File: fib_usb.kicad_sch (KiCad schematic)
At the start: 0 parts

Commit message: added several ICs, implementted schematics for charger, boost converter and LDOs
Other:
- note added: "TYPE-A 2.0"
- note added: "TYPE-C 2.0 DEBUG"
- note added: "TYPE-C HS DP"
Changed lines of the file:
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@@
 	(generator_version "8.0")
 	(paper "A4")
+	(text "TYPE-A 2.0"
+		(exclude_from_sim no)
+		(at 45.974 75.438 0)
+		(effects
+			(font
+				(size 1.27 1.27)
+			)
+		)
+	)
+	(text "TYPE-C HS DP"
+		(exclude_from_sim no)
+		(at 46.99 54.102 0)
+		(effects
+			(font
+				(size 1.27 1.27)
+			)
+		)
+	)
+	(text "TYPE-C 2.0 DEBUG"
+		(exclude_from_sim no)
+		(at 45.466 89.408 0)
+		(effects
+			(font
+				(size 1.27 1.27)
+			)
+		)
+	)
 )

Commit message: added usb+PD+DP & pcie implementations from antmicro design, added specs for USB components, rethought power+usb arch
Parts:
- added C100, C98: C_1u_16V_0402, jetson-orin-baseboard-footprints:C_0402_1005Metric, symbol jetson-orin-baseboard:C_1u_16V_0402
- added C56, C59, C67, C68, C80, C86, C96: C_10u_0402, jetson-orin-baseboard-footprints:C_0402_1005Metric, symbol jetson-orin-baseboard:C_10u_0402
- added C57, C70, C71, C72, C73, C74, C75, C76, C77, C78, C81, C82, C83, C84, C85, C89, C90, C91, C92, C94, C95, C97, C99: C_100n_0402, jetson-orin-baseboard-footprints:C_0402_1005Metric, symbol jetson-orin-baseboard:C_100n_0402
- added C69: C_10u_25V_0603, jetson-orin-baseboard-footprints:C_0603_1608Metric, symbol jetson-orin-baseboard:C_10u_25V_0603
- added C79, C93: C_4u7_25V_0402, jetson-orin-baseboard-footprints:C_0402_1005Metric, symbol jetson-orin-baseboard:C_4u7_25V_0402
- added C87, C88: C_47p_0402, jetson-orin-baseboard-footprints:C_0402_1005Metric, symbol jetson-orin-baseboard:C_47p_0402
- added D10, D12, D14, D7, D8, D9: LED_G_0603_LTST-C190GKT, jetson-orin-baseboard-footprints:LED_0603_1608Metric_G, symbol jetson-orin-baseboard:LED_G_0603_LTST-C190GKT
- added D11, D13: DF2S30FS_SOD, jetson-orin-baseboard-footprints:SOD-923, symbol jetson-orin-baseboard:DF2S30FS_SOD
- added D6: RB521S30T1G, jetson-orin-baseboard-footprints:SOD-523, symbol jetson-orin-baseboard:RB521S30T1G
- added J12: Conn_USB-C_WE_632723300011, jetson-orin-baseboard-footprints:Conn_USB-C_WE_632723300011, symbol jetson-orin-baseboard:USB-C_WE_632723300011
- added J8: USB-C_USB4105-GF-A, jetson-orin-baseboard-footprints:USB-C_GCT_USB4105-GF-A, symbol jetson-orin-baseboard:USB-C_GCT_USB4105-GF-A
- added R15, R17, R20, R52, R54, R60, R77: R_10k_0402, jetson-orin-baseboard-footprints:R_0402_1005Metric, symbol jetson-orin-baseboard:R_10k_0402
- added R16, R18, R48, R49: R_100k_0402, jetson-orin-baseboard-footprints:R_0402_1005Metric, symbol jetson-orin-baseboard:R_100k_0402
- added R19, R31, R32, R33, R34, R38, R41, R42, R43, R50, R51, R53, R55, R56, R75, R76: R_0R_0402, jetson-orin-baseboard-footprints:R_0402_1005Metric, symbol jetson-orin-baseboard:R_0R_0402
- added R27, R61, R62, R63, R64, R65, R66, R67, R68, R69, R70, R71, R72, R73, R74: R_1k_0402, jetson-orin-baseboard-footprints:R_0402_1005Metric, symbol jetson-orin-baseboard:R_1k_0402
- added R35, R36, R46, R47, R78, R98: R_4k7_0402, jetson-orin-baseboard-footprints:R_0402_1005Metric, symbol jetson-orin-baseboard:R_4k7_0402
- added R37: R_4x0R_0201_array, jetson-orin-baseboard-footprints:R_Array_4x0201_Panasonic_EXB18V, symbol jetson-orin-baseboard:R_4x0R_0201_array
- added R39, R40, R44, R45: R_200R_0402, jetson-orin-baseboard-footprints:R_0402_1005Metric, symbol jetson-orin-baseboard:R_200R_0402
- added R57, R79: R_2k2_0402, jetson-orin-baseboard-footprints:R_0402_1005Metric, symbol jetson-orin-baseboard:R_2k2_0402
- added R58, R59: R_27R_0402, jetson-orin-baseboard-footprints:R_0402_1005Metric, symbol jetson-orin-baseboard:R_27R_0402
- added R80, R97: R_2M_0402, jetson-orin-baseboard-footprints:R_0402_1005Metric, symbol jetson-orin-baseboard:R_2M_0402
- added TP1, TP10, TP11, TP2, TP3, TP4, TP5, TP6, TP7, TP8, TP9: TP_0.75mm_SMD, jetson-orin-baseboard-footprints:TP_SMD_0.75mm, symbol jetson-orin-baseboard:TP_0.75mm_SMD
- added U10: W25Q80DV_USON, jetson-orin-baseboard-footprints:USON-8_2x3mm_P0.5mm, symbol jetson-orin-baseboard:W25Q80DV_USON
- added U11, U13: AP22615A_TSOT26, jetson-orin-baseboard-footprints:TSOT23-6, symbol jetson-orin-baseboard:AP22615A_TSOT26
- added U12: TUSB1046-DCIRNQ, jetson-orin-baseboard-footprints:WQFN-40_1EP_6x3mm_Pitch0.4mm_EP4.7x2.7mm, symbol jetson-orin-baseboard:TUSB1046-DCIRNQ
- added U14, U15, U16, U17, U18: TPD4E05U06QDQARQ1, jetson-orin-baseboard-footprints:USON-10_2.5x1mm_P0.5mm, symbol jetson-orin-baseboard:TPD4E05U06QDQARQ1
- added U7: NCP730BMT330_WSON, jetson-orin-baseboard-footprints:WSON-6-1EP_2x2mm_P0.65mm, symbol jetson-orin-baseboard:NCP730BMT330_WSON
- added U8: TPS65988DHRSHR, jetson-orin-baseboard-footprints:IC_TPS65987DDHRSHR, symbol jetson-orin-baseboard:TPS65988DHRSHR
- added U9: FT230X_QFN, jetson-orin-baseboard-footprints:QFN-16-1EP_4x4mm_P0.65mm, symbol jetson-orin-baseboard:FT230X_QFN
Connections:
- new net: C72.1, R20.2, U9.9 (~{RESET})
- new net: R57.2, U11.5 (ISET)
- new net: R34.2, U9.4 (~{CTS})
- new net: D8.1, R39.2
- new net: TP9.1, U8.30 (GPIO3/HPD1)
- new net: D12.1, R78.2
- new net: TP11.1, U12.29 (CAD_SNK/RSVD1)
- new net: D9.1, R40.2
- new net: R53.2, R54.2, U11.4 (EN)
- new net: R31.2, U9.15 (TXD)
- new net: D7.1, R44.1
- new net: R79.2, U13.5 (ISET)
- new net: R32.2, U9.2 (RXD)
- new net: D10.1, R45.1
- new net: R76.2, R77.2, U13.4 (EN)
- new net: R33.2, U9.16 (~{RTS})
- new net: U14.4, U14.7
- new net: U14.5, U14.6
- new net: D14.1, R98.1
- new net +3V3: C56.1, C57.1, C74.1, C76.1, C78.1, C85.1, C86.1, R35.1, R36.1, R46.1, R47.1, R49.2, R60.2, R61.2, R63.2, R65.2, R67.2, R69.2, R71.2, R73.2, U12.1 (VCC), U12.20 (VCC), U12.28 (VCC), U12.6 (VCC), U8.5 (VIN_3V3)
- new net +5V: C75.1, C80.2, C90.1, C96.1, R50.2, R52.2, R75.2, U11.6 (IN), U13.6 (IN), U8.25 (PP1_CABLE), U8.46 (PP2_CABLE)
- new net DEBUG_RXD: R31.1
- new net DEBUG_TXD: R32.1
- new net DP1_AUX_N: R49.1, U12.25 (AUX_N)
- new net DP1_AUX_P: R48.1, U12.24 (AUX_P)
- new net DP1_TXD0_N: U12.10 (DP0_N)
- new net DP1_TXD0_P: U12.9 (DP0_P)
- new net DP1_TXD1_N: U12.13 (DP1_N)
- new net DP1_TXD1_P: U12.12 (DP1_P)
- new net DP1_TXD2_N: U12.16 (DP2_N)
- new net DP1_TXD2_P: U12.15 (DP2_P)
- new net DP1_TXD3_N: U12.19 (DP3_N)
- new net DP1_TXD3_P: U12.18 (DP3_P)
- new net DRAIN1: U8.52 (DRAIN2), U8.56 (DRAIN2), U8.57 (DRAIN2), U8.7 (DRAIN2)
- new net DRAIN2: U8.15 (DRAIN1), U8.19 (DRAIN1), U8.58 (DRAIN1), U8.8 (DRAIN1)
- new net EEPROM_PWR: C73.2, D6.1, R27.1, U10.3 (~{WP}/IO2), U10.7 (~{HOLD}/IO3), U10.8 (VCC)
- new net FTDI_3V3: C68.1, C70.1, C71.1, R20.1, R44.2, R45.2, U7.1 (V_{OUT}), U9.1 (V_{CCIO}), U9.10 (V_{CC}), U9.8 (3V3_{OUT})
- new net FTDI_CBUS0: TP1.1, U9.12 (CBUS0)
- new net FTDI_CBUS3: TP2.1, U9.14 (CBUS3)
- new net FTDI_LED_RX: D7.2, U9.11 (CBUS1)
- new net FTDI_LED_TX: D10.2, U9.5 (CBUS2)
- new net GND: C100.1, C56.2, C57.2, C59.2, C67.2, C68.2, C69.2, C70.2, C71.2, C72.2, C73.1, C74.2, C75.2, C76.2, C77.2, C78.2, C79.2, C80.1, C85.2, C86.2, C87.1, C88.2, C89.2, C90.2, C93.2, C96.2, C97.2, C98.2, C99.2, D11.2, D12.2, D13.2, D14.2, D8.2, D9.2, J12.A1 (GND), J12.A12 (GND), J12.B1 (GND), J12.B12 (GND), J12.SH, J8.A1 (GND), J8.A12 (GND), J8.B1 (GND), J8.B12 (GND), J8.SH (SHIELD), R16.1, R18.1, R19.1, R48.2, R54.1, R57.1, R62.2, R64.2, R66.2, R68.2, R70.2, R72.2, R74.2, R77.1, R79.1, R80.2, R97.2, U10.4 (VSS), U11.2 (GND), U12.41 (GND), U13.2 (GND), U14.3, U14.8, U15.3, U15.8, U16.3, U16.8, U17.3, U17.8, U18.3, U18.8, U7.3 (GND), U7.5 (PG), U7.7 (GND), U8.20 (GND), U8.51 (GND), U8.59 (GND_EP), U9.13 (GND), U9.17 (GND), U9.3 (GND)
- new net GPIO010: R41.1
- new net HPDIN: R51.2, U12.32 (HPDIN/RSVD2)
- new net PDC_ADCIN1: R15.2, R16.2, U8.6 (ADCIN1)
- new net PDC_ADCIN2: R17.2, R18.2, U8.10 (ADCIN2)
- new net PDC_CTL0: R37.2 (R2.1), U8.17 (GPIO1)
- new net PDC_CTL1: R37.1 (R1.1), U8.18 (GPIO2)
- new net PDC_FLIP: R37.3 (R3.1), U8.16 (GPIO0)
- new net PDC_GPIO14: R39.1, U8.42 (GPIO14/PWM1)
- new net PDC_GPIO15: R40.1, U8.43 (GPIO15/PWM2)
- new net PDC_HPD2: R38.2, U8.31 (GPIO4/HPD2)
- new net PDC_I2C1_IRQn: R41.2, U8.29 (~{I2C1_IRQ})
- new net PDC_I2C1_SCL: R42.2, R47.2, U8.27 (I2C1_SCL)
- new net PDC_I2C1_SDA: R43.2, R46.2, U8.28 (I2C1_SDA)
- new net PDC_I2C2_IRQn: TP3.1, U8.34 (~{I2C2_IRQ})
- new net PDC_I2C2_SCL: R36.2, TP4.1, U8.32 (I2C2_SCL)
- new net PDC_I2C2_SDA: R35.2, TP5.1, U8.33 (I2C2_SDA)
- new net PDC_I2C3_SCL: TP6.1, U8.21 (I2C3_SCL/GPIO5)
- new net PDC_I2C3_SDA: TP7.1, U8.22 (I2C3_SDA/GPIO6)
- new net PDC_LDO_1V8: C59.1, U8.35 (LDO_1V8)
- new net PDC_LDO_3V3: C67.1, D6.2, R15.1, R17.1, U8.9 (LDO_3V3)
- new net PDC_MISO: R27.2, U10.2 (SO/IO1), U8.36 (SPI_POCI/GPIO8)
- new net PDC_MOSI: U10.5 (SI/IO0), U8.37 (SPI_PICO/GPIO9)
- new net PDC_RESET: R19.2, U8.44 (HRESET)
- new net PDC_SCLK: U10.6 (SCLK), U8.38 (SPI_CLK/GPIO10)
- new net PWR_SOFT: R33.1
- new net SYS_SCL: R42.1, R56.2
- new net SYS_SDA: R43.1, R55.2
- new net USB2_D_N: J12.A7 (D-), J12.B7 (D-), U18.4, U18.7
- new net USB2_D_P: J12.A6 (D+), J12.B6 (D+), U18.2, U18.9
- new net USBC0_5V_PEN: R75.1, R76.1, U8.49 (GPIO17/PP_EXT2)
- new net USBC0_CC1: J12.A5 (CC1), U18.1, U18.10, U8.45 (C2_CC1)
- new net USBC0_CC2: J12.B5 (CC2), U18.5, U18.6, U8.47 (C2_CC2)
- new net USBC0_CONN_TX1_N: C94.2, J12.A3 (TX1-), U17.5, U17.6
- new net USBC0_CONN_TX1_P: C91.2, J12.A2 (TX1+), U17.4, U17.7
- new net USBC0_CONN_TX2_N: C95.2, J12.B3 (TX2-), U16.4, U16.7
- new net USBC0_CONN_TX2_P: C92.2, J12.B2 (TX2+), U16.5, U16.6
- new net USBC0_CTL0: R37.7 (R2.2), R55.1, U12.22 (CTL0/SDA)
- new net USBC0_CTL1: R37.8 (R1.2), U12.23 (CTL1/HPDIN)
- new net USBC0_DPEQ0: R67.1, R68.1, U12.14 (DPEQ0/A1)
- new net USBC0_DPEQ1: R69.1, R70.1, U12.2 (DPEQ1)
- new net USBC0_EQ0: R71.1, R72.1, U12.38 (EQ0)
- new net USBC0_EQ1: R73.1, R74.1, U12.35 (EQ1)
- new net USBC0_FLG: R60.1, U13.3 (FLG)
- new net USBC0_FLIP: R37.6 (R3.2), R56.1, U12.21 (FLIP/SCL)
- new net USBC0_I2C_EN: R61.1, R62.1, U12.17 (I2C_EN)
- new net USBC0_RX1_N: J12.B10 (RX1-), U12.31 (RX1_N), U17.2, U17.9
- new net USBC0_RX1_P: J12.B11 (RX1+), U12.30 (RX1_P), U17.1, U17.10
- new net USBC0_RX2_N: J12.A10 (RX2-), U12.39 (RX2_N), U16.1, U16.10
- new net USBC0_RX2_P: J12.A11 (RX2+), U12.40 (RX2_P), U16.2, U16.9
- new net USBC0_SBU_N: J12.A8 (SBU1), R80.1, U12.27 (SBU1), U14.2, U14.9
- new net USBC0_SBU_P: J12.B8 (SBU2), R97.1, U12.26 (SBU2), U14.1, U14.10
- new net USBC0_SSEQ0: R63.1, R64.1, U12.11 (SSEQ0/A0)
- new net USBC0_SSEQ1: R65.1, R66.1, U12.3 (SSEQ1)
- new net USBC0_TX1_N: C94.1, U12.34 (TX1_N)
- new net USBC0_TX1_P: C91.1, U12.33 (TX1_P)
- new net USBC0_TX2_N: C95.1, U12.36 (TX2_N)
- new net USBC0_TX2_P: C92.1, U12.37 (TX2_P)
- new net USBC0_VBUS: C100.2, C99.1, D13.1, J12.A4 (VBUS), J12.A9 (VBUS), J12.B4 (VBUS), J12.B9 (VBUS), R98.2, U13.1 (OUT), U8.3 (VBUS2)
- new net USBC3_5V_PEN: R50.1, R53.1, U8.48 (GPIO16/PP_EXT1)
- new net USBC3_CC1: J8.A5 (CC1), U15.1, U15.10, U8.24 (C1_CC1)
- new net USBC3_CC2: J8.B5 (CC2), U15.5, U15.6, U8.26 (C1_CC2)
- new net USBC3_D_N: C87.2, J8.A7 (D-), J8.B7 (D-), R59.2, U15.4, U15.7
- new net USBC3_D_P: C88.1, J8.A6 (D+), J8.B6 (D+), R58.2, U15.2, U15.9
- new net USBC3_FLG: R52.1, TP10.1, U11.3 (FLG)
- new net USBC3_VBUS: C69.1, C97.1, C98.1, D11.1, J8.A4 (VBUS), J8.A9 (VBUS), J8.B4 (VBUS), J8.B9 (VBUS), R78.1, U11.1 (OUT), U7.4 (EN), U7.6 (V_{IN}), U8.13 (VBUS1)
- new net USBC_HPD: R38.1, R51.1
- new net USBPD1_HV: C77.1, C79.1, U8.11 (PP_HV1)
- new net USBPD2_HV: C89.1, C93.1, U8.1 (PP_HV2)
- new net USBSS0_RX_C_N: C81.2, U12.4 (SSRX_N)
- new net USBSS0_RX_C_P: C83.2, U12.5 (SSRX_P)
- new net USBSS0_RX_N: C83.1
- new net USBSS0_RX_P: C81.1
- new net USBSS0_TX_C_N: C82.2, U12.7 (SSTX_N)
- new net USBSS0_TX_C_P: C84.2, U12.8 (SSTX_P)
- new net USBSS0_TX_N: C84.1
- new net USBSS0_TX_P: C82.1
- new net USB_FTDI_N: R59.1, U9.7 (D-)
- new net USB_FTDI_P: R58.1, U9.6 (D+)
- new net ~{PDC_CS}: U10.1 (~{CS}), U8.39 (~{SPI_CS}/GPIO11)
- new net ~{PDC_I2C3_IRQ}: TP8.1, U8.23 (~{I2C3_IRQ}/GPIO7)
- no-connect marks 0 -> 14
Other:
- note added: "4 LANE DP"
- note added: "CONFIGURATION"
- note added: "CTL0"
- note added: "CTL1"
- note added: "H"
- note added: "L"
- note added: "POWER DOWN"
- note added: "RX"
- note added: "TX"
- note added: "USB + 2 LANE DP"
- note added: "USB ONLY"
- note added: "USBC0"
- note added: "USBC3"
- note removed: "TYPE-A 2.0"
- note removed: "TYPE-C 2.0 DEBUG"
- note removed: "TYPE-C HS DP"

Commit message: added nets for 40 pin headers (epd & rpi header) connected some of the nets i'm reeusing
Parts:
- added R427, R428, R431, R433, R434, R439, R442, R463, R464, R466, R467, R468, R469, R470, R471, R472: 0R, Resistor_SMD:R_0603_1608Metric, symbol Device:R_Small
- C401: renamed from C56; value C_10u_0402 -> 10uF; footprint jetson-orin-baseboard-footprints:C_0402_1005Metric -> Capacitor_SMD:C_0603_1608Metric
- C402: renamed from C57; value C_100n_0402 -> 100nF; footprint jetson-orin-baseboard-footprints:C_0402_1005Metric -> Capacitor_SMD:C_0603_1608Metric
- C403: renamed from C59; value C_10u_0402 -> 10uF; footprint jetson-orin-baseboard-footprints:C_0402_1005Metric -> Capacitor_SMD:C_0603_1608Metric
- C404: renamed from C68; value C_10u_0402 -> 10uF; footprint jetson-orin-baseboard-footprints:C_0402_1005Metric -> Capacitor_SMD:C_0603_1608Metric
- C405: renamed from C67; value C_10u_0402 -> 10uF; footprint jetson-orin-baseboard-footprints:C_0402_1005Metric -> Capacitor_SMD:C_0603_1608Metric
- C406: renamed from C69; value C_10u_25V_0603 -> 10uF 25V; footprint jetson-orin-baseboard-footprints:C_0603_1608Metric -> Capacitor_SMD:C_0603_1608Metric
- C407: renamed from C70; value C_100n_0402 -> 100nF; footprint jetson-orin-baseboard-footprints:C_0402_1005Metric -> Capacitor_SMD:C_0603_1608Metric
- C408: renamed from C71; value C_100n_0402 -> 100nF; footprint jetson-orin-baseboard-footprints:C_0402_1005Metric -> Capacitor_SMD:C_0603_1608Metric
- C409: renamed from C72; value C_100n_0402 -> 100nF; footprint jetson-orin-baseboard-footprints:C_0402_1005Metric -> Capacitor_SMD:C_0603_1608Metric
- C410: renamed from C75; value C_100n_0402 -> 100nF; footprint jetson-orin-baseboard-footprints:C_0402_1005Metric -> Capacitor_SMD:C_0603_1608Metric
- C411: renamed from C77; value C_100n_0402 -> 100nF; footprint jetson-orin-baseboard-footprints:C_0402_1005Metric -> Capacitor_SMD:C_0603_1608Metric
- C412: renamed from C79; value C_4u7_25V_0402 -> 4.7uF; footprint jetson-orin-baseboard-footprints:C_0402_1005Metric -> Capacitor_SMD:C_0603_1608Metric
- C413: renamed from C80; value C_10u_0402 -> 10uF; footprint jetson-orin-baseboard-footprints:C_0402_1005Metric -> Capacitor_SMD:C_0603_1608Metric
- C414: renamed from C74; value C_100n_0402 -> 100nF; footprint jetson-orin-baseboard-footprints:C_0402_1005Metric -> Capacitor_SMD:C_0603_1608Metric
- C415: renamed from C76; value C_100n_0402 -> 100nF; footprint jetson-orin-baseboard-footprints:C_0402_1005Metric -> Capacitor_SMD:C_0603_1608Metric
- C416: renamed from C78; value C_100n_0402 -> 100nF; footprint jetson-orin-baseboard-footprints:C_0402_1005Metric -> Capacitor_SMD:C_0603_1608Metric
- C417: renamed from C81; value C_100n_0402 -> 100nF; footprint jetson-orin-baseboard-footprints:C_0402_1005Metric -> Capacitor_SMD:C_0603_1608Metric
- C418: renamed from C82; value C_100n_0402 -> 100nF; footprint jetson-orin-baseboard-footprints:C_0402_1005Metric -> Capacitor_SMD:C_0603_1608Metric
- C419: renamed from C83; value C_100n_0402 -> 100nF; footprint jetson-orin-baseboard-footprints:C_0402_1005Metric -> Capacitor_SMD:C_0603_1608Metric
- C420: renamed from C84; value C_100n_0402 -> 100nF; footprint jetson-orin-baseboard-footprints:C_0402_1005Metric -> Capacitor_SMD:C_0603_1608Metric
- C421: renamed from C85; value C_100n_0402 -> 100nF; footprint jetson-orin-baseboard-footprints:C_0402_1005Metric -> Capacitor_SMD:C_0603_1608Metric
- C422: renamed from C86; value C_10u_0402 -> 10uF; footprint jetson-orin-baseboard-footprints:C_0402_1005Metric -> Capacitor_SMD:C_0603_1608Metric
- C423: renamed from C87; value C_47p_0402 -> 47pF; footprint jetson-orin-baseboard-footprints:C_0402_1005Metric -> Capacitor_SMD:C_0603_1608Metric
- C424: renamed from C88; value C_47p_0402 -> 47pF; footprint jetson-orin-baseboard-footprints:C_0402_1005Metric -> Capacitor_SMD:C_0603_1608Metric
- C425: renamed from C89; value C_100n_0402 -> 100nF; footprint jetson-orin-baseboard-footprints:C_0402_1005Metric -> Capacitor_SMD:C_0603_1608Metric
- C426: renamed from C90; value C_100n_0402 -> 100nF; footprint jetson-orin-baseboard-footprints:C_0402_1005Metric -> Capacitor_SMD:C_0603_1608Metric
- C427: renamed from C93; value C_4u7_25V_0402 -> 4.7uF; footprint jetson-orin-baseboard-footprints:C_0402_1005Metric -> Capacitor_SMD:C_0603_1608Metric
- C428: renamed from C96; value C_10u_0402 -> 10uF; footprint jetson-orin-baseboard-footprints:C_0402_1005Metric -> Capacitor_SMD:C_0603_1608Metric
- C429: renamed from C97; value C_100n_0402 -> 100nF; footprint jetson-orin-baseboard-footprints:C_0402_1005Metric -> Capacitor_SMD:C_0603_1608Metric
- C430: renamed from C91; value C_100n_0402 -> 100nF; footprint jetson-orin-baseboard-footprints:C_0402_1005Metric -> Capacitor_SMD:C_0603_1608Metric
- C431: renamed from C92; value C_100n_0402 -> 100nF; footprint jetson-orin-baseboard-footprints:C_0402_1005Metric -> Capacitor_SMD:C_0603_1608Metric
- C432: renamed from C94; value C_100n_0402 -> 100nF; footprint jetson-orin-baseboard-footprints:C_0402_1005Metric -> Capacitor_SMD:C_0603_1608Metric
- C433: renamed from C95; value C_100n_0402 -> 100nF; footprint jetson-orin-baseboard-footprints:C_0402_1005Metric -> Capacitor_SMD:C_0603_1608Metric
- C434: renamed from C98; value C_1u_16V_0402 -> 1uF 16V; footprint jetson-orin-baseboard-footprints:C_0402_1005Metric -> Capacitor_SMD:C_0603_1608Metric
- C435: renamed from C73; value C_100n_0402 -> 100nF; footprint jetson-orin-baseboard-footprints:C_0402_1005Metric -> Capacitor_SMD:C_0603_1608Metric
- C436: renamed from C99; value C_100n_0402 -> 100nF; footprint jetson-orin-baseboard-footprints:C_0402_1005Metric -> Capacitor_SMD:C_0603_1608Metric
- C437: renamed from C100; value C_1u_16V_0402 -> 1uF 16V; footprint jetson-orin-baseboard-footprints:C_0402_1005Metric -> Capacitor_SMD:C_0603_1608Metric
- R401: renamed from R15; value R_10k_0402 -> 10K; footprint jetson-orin-baseboard-footprints:R_0402_1005Metric -> Resistor_SMD:R_0603_1608Metric
- R402: renamed from R16; value R_100k_0402 -> 100K; footprint jetson-orin-baseboard-footprints:R_0402_1005Metric -> Resistor_SMD:R_0603_1608Metric
- R403: renamed from R17; value R_10k_0402 -> 10K; footprint jetson-orin-baseboard-footprints:R_0402_1005Metric -> Resistor_SMD:R_0603_1608Metric
- R404: renamed from R18; value R_100k_0402 -> 100K; footprint jetson-orin-baseboard-footprints:R_0402_1005Metric -> Resistor_SMD:R_0603_1608Metric
- R405: renamed from R19; value R_0R_0402 -> 0R; footprint jetson-orin-baseboard-footprints:R_0402_1005Metric -> Resistor_SMD:R_0603_1608Metric
- R406: renamed from R20; value R_10k_0402 -> 10K; footprint jetson-orin-baseboard-footprints:R_0402_1005Metric -> Resistor_SMD:R_0603_1608Metric
- R407: renamed from R31; value R_0R_0402 -> 0R; footprint jetson-orin-baseboard-footprints:R_0402_1005Metric -> Resistor_SMD:R_0603_1608Metric
- R408: renamed from R32; value R_0R_0402 -> 0R; footprint jetson-orin-baseboard-footprints:R_0402_1005Metric -> Resistor_SMD:R_0603_1608Metric
- R409: renamed from R33; value R_0R_0402 -> 0R; footprint jetson-orin-baseboard-footprints:R_0402_1005Metric -> Resistor_SMD:R_0603_1608Metric
- R410: renamed from R34; value R_0R_0402 -> 0R; footprint jetson-orin-baseboard-footprints:R_0402_1005Metric -> Resistor_SMD:R_0603_1608Metric
- R411: renamed from R50; value R_0R_0402 -> 0R; footprint jetson-orin-baseboard-footprints:R_0402_1005Metric -> Resistor_SMD:R_0603_1608Metric
- R412: renamed from R52; value R_10k_0402 -> 10K; footprint jetson-orin-baseboard-footprints:R_0402_1005Metric -> Resistor_SMD:R_0603_1608Metric
- R413: renamed from R53; value R_0R_0402 -> 0R; footprint jetson-orin-baseboard-footprints:R_0402_1005Metric -> Resistor_SMD:R_0603_1608Metric
- R415: renamed from R54; value R_10k_0402 -> 10K; footprint jetson-orin-baseboard-footprints:R_0402_1005Metric -> Resistor_SMD:R_0603_1608Metric
- R416: renamed from R38; value R_0R_0402 -> 0R; footprint jetson-orin-baseboard-footprints:R_0402_1005Metric -> Resistor_SMD:R_0603_1608Metric
- R417: renamed from R39; value R_200R_0402 -> 200R; footprint jetson-orin-baseboard-footprints:R_0402_1005Metric -> Resistor_SMD:R_0603_1608Metric
- R418: renamed from R40; value R_200R_0402 -> 200R; footprint jetson-orin-baseboard-footprints:R_0402_1005Metric -> Resistor_SMD:R_0603_1608Metric
- R419: renamed from R41; value R_0R_0402 -> 0R; footprint jetson-orin-baseboard-footprints:R_0402_1005Metric -> Resistor_SMD:R_0603_1608Metric
- R420: renamed from R42; value R_0R_0402 -> 0R; footprint jetson-orin-baseboard-footprints:R_0402_1005Metric -> Resistor_SMD:R_0603_1608Metric
- R421: renamed from R43; value R_0R_0402 -> 0R; footprint jetson-orin-baseboard-footprints:R_0402_1005Metric -> Resistor_SMD:R_0603_1608Metric
- R422: renamed from R44; value R_200R_0402 -> 200R; footprint jetson-orin-baseboard-footprints:R_0402_1005Metric -> Resistor_SMD:R_0603_1608Metric
- R423: renamed from R45; value R_200R_0402 -> 200R; footprint jetson-orin-baseboard-footprints:R_0402_1005Metric -> Resistor_SMD:R_0603_1608Metric
- R424: renamed from R57; value R_2k2_0402 -> 2.2K; footprint jetson-orin-baseboard-footprints:R_0402_1005Metric -> Resistor_SMD:R_0603_1608Metric
- R425: renamed from R58; value R_27R_0402 -> 27R; footprint jetson-orin-baseboard-footprints:R_0402_1005Metric -> Resistor_SMD:R_0603_1608Metric
- R426: renamed from R59; value R_27R_0402 -> 27R; footprint jetson-orin-baseboard-footprints:R_0402_1005Metric -> Resistor_SMD:R_0603_1608Metric
- R429: renamed from R48; value R_100k_0402 -> 100K; footprint jetson-orin-baseboard-footprints:R_0402_1005Metric -> Resistor_SMD:R_0603_1608Metric
- R430: renamed from R49; value R_100k_0402 -> 100K; footprint jetson-orin-baseboard-footprints:R_0402_1005Metric -> Resistor_SMD:R_0603_1608Metric
- R432: renamed from R51; value R_0R_0402 -> 0R; footprint jetson-orin-baseboard-footprints:R_0402_1005Metric -> Resistor_SMD:R_0603_1608Metric
- R435: renamed from R46; value R_4k7_0402 -> 4.7K; footprint jetson-orin-baseboard-footprints:R_0402_1005Metric -> Resistor_SMD:R_0603_1608Metric
- R436: renamed from R47; value R_4k7_0402 -> 4.7K; footprint jetson-orin-baseboard-footprints:R_0402_1005Metric -> Resistor_SMD:R_0603_1608Metric
- R437: renamed from R35; value R_4k7_0402 -> 4.7K; footprint jetson-orin-baseboard-footprints:R_0402_1005Metric -> Resistor_SMD:R_0603_1608Metric
- R438: renamed from R36; value R_4k7_0402 -> 4.7K; footprint jetson-orin-baseboard-footprints:R_0402_1005Metric -> Resistor_SMD:R_0603_1608Metric
- R440: renamed from R55; value R_0R_0402 -> 0R; footprint jetson-orin-baseboard-footprints:R_0402_1005Metric -> Resistor_SMD:R_0603_1608Metric
- R441: renamed from R56; value R_0R_0402 -> 0R; footprint jetson-orin-baseboard-footprints:R_0402_1005Metric -> Resistor_SMD:R_0603_1608Metric
- R443: renamed from R60; value R_10k_0402 -> 10K; footprint jetson-orin-baseboard-footprints:R_0402_1005Metric -> Resistor_SMD:R_0603_1608Metric
- R444: renamed from R75; value R_0R_0402 -> 0R; footprint jetson-orin-baseboard-footprints:R_0402_1005Metric -> Resistor_SMD:R_0603_1608Metric
- R445: renamed from R76; value R_0R_0402 -> 0R; footprint jetson-orin-baseboard-footprints:R_0402_1005Metric -> Resistor_SMD:R_0603_1608Metric
- R446: renamed from R77; value R_10k_0402 -> 10K; footprint jetson-orin-baseboard-footprints:R_0402_1005Metric -> Resistor_SMD:R_0603_1608Metric
- R447: renamed from R61; value R_1k_0402 -> 2K; footprint jetson-orin-baseboard-footprints:R_0402_1005Metric -> Resistor_SMD:R_0603_1608Metric
- R448: renamed from R62; value R_1k_0402 -> 1K; footprint jetson-orin-baseboard-footprints:R_0402_1005Metric -> Resistor_SMD:R_0603_1608Metric
- R449: renamed from R63; value R_1k_0402 -> 2K; footprint jetson-orin-baseboard-footprints:R_0402_1005Metric -> Resistor_SMD:R_0603_1608Metric
- R450: renamed from R64; value R_1k_0402 -> 2K; footprint jetson-orin-baseboard-footprints:R_0402_1005Metric -> Resistor_SMD:R_0603_1608Metric
- R451: renamed from R65; value R_1k_0402 -> 2K; footprint jetson-orin-baseboard-footprints:R_0402_1005Metric -> Resistor_SMD:R_0603_1608Metric
- R452: renamed from R66; value R_1k_0402 -> 1K; footprint jetson-orin-baseboard-footprints:R_0402_1005Metric -> Resistor_SMD:R_0603_1608Metric
- R453: renamed from R67; value R_1k_0402 -> 2K; footprint jetson-orin-baseboard-footprints:R_0402_1005Metric -> Resistor_SMD:R_0603_1608Metric
- R454: renamed from R68; value R_1k_0402 -> 2K; footprint jetson-orin-baseboard-footprints:R_0402_1005Metric -> Resistor_SMD:R_0603_1608Metric
- R455: renamed from R69; value R_1k_0402 -> 2K; footprint jetson-orin-baseboard-footprints:R_0402_1005Metric -> Resistor_SMD:R_0603_1608Metric
- R456: renamed from R70; value R_1k_0402 -> 1K; footprint jetson-orin-baseboard-footprints:R_0402_1005Metric -> Resistor_SMD:R_0603_1608Metric
- R457: renamed from R71; value R_1k_0402 -> 2K; footprint jetson-orin-baseboard-footprints:R_0402_1005Metric -> Resistor_SMD:R_0603_1608Metric
- R458: renamed from R72; value R_1k_0402 -> 2K; footprint jetson-orin-baseboard-footprints:R_0402_1005Metric -> Resistor_SMD:R_0603_1608Metric
- R459: renamed from R73; value R_1k_0402 -> 2K; footprint jetson-orin-baseboard-footprints:R_0402_1005Metric -> Resistor_SMD:R_0603_1608Metric
- R460: renamed from R74; value R_1k_0402 -> 1K; footprint jetson-orin-baseboard-footprints:R_0402_1005Metric -> Resistor_SMD:R_0603_1608Metric
- R461: renamed from R79; value R_2k2_0402 -> 2.2K; footprint jetson-orin-baseboard-footprints:R_0402_1005Metric -> Resistor_SMD:R_0603_1608Metric
- R462: renamed from R78; value R_4k7_0402 -> 4.7K; footprint jetson-orin-baseboard-footprints:R_0402_1005Metric -> Resistor_SMD:R_0603_1608Metric
- R465: renamed from R27; value R_1k_0402 -> 1K; footprint jetson-orin-baseboard-footprints:R_0402_1005Metric -> Resistor_SMD:R_0603_1608Metric
- R473: renamed from R80; value R_2M_0402 -> 3M; footprint jetson-orin-baseboard-footprints:R_0402_1005Metric -> Resistor_SMD:R_0603_1608Metric
- R474: renamed from R97; value R_2M_0402 -> 3M; footprint jetson-orin-baseboard-footprints:R_0402_1005Metric -> Resistor_SMD:R_0603_1608Metric
- R475: renamed from R98; value R_4k7_0402 -> 4.7K; footprint jetson-orin-baseboard-footprints:R_0402_1005Metric -> Resistor_SMD:R_0603_1608Metric
- TP401: renamed from TP1; footprint jetson-orin-baseboard-footprints:TP_SMD_0.75mm -> TestPoint:TestPoint_Pad_D1.0mm
- TP402: renamed from TP2; footprint jetson-orin-baseboard-footprints:TP_SMD_0.75mm -> TestPoint:TestPoint_Pad_D1.0mm
- TP403: renamed from TP10; footprint jetson-orin-baseboard-footprints:TP_SMD_0.75mm -> TestPoint:TestPoint_Pad_D1.0mm
- TP404: renamed from TP3; footprint jetson-orin-baseboard-footprints:TP_SMD_0.75mm -> TestPoint:TestPoint_Pad_D1.0mm
- TP405: renamed from TP4; footprint jetson-orin-baseboard-footprints:TP_SMD_0.75mm -> TestPoint:TestPoint_Pad_D1.0mm
- TP406: renamed from TP5; footprint jetson-orin-baseboard-footprints:TP_SMD_0.75mm -> TestPoint:TestPoint_Pad_D1.0mm
- TP407: renamed from TP6; footprint jetson-orin-baseboard-footprints:TP_SMD_0.75mm -> TestPoint:TestPoint_Pad_D1.0mm
- TP408: renamed from TP7; footprint jetson-orin-baseboard-footprints:TP_SMD_0.75mm -> TestPoint:TestPoint_Pad_D1.0mm
- TP409: renamed from TP8; footprint jetson-orin-baseboard-footprints:TP_SMD_0.75mm -> TestPoint:TestPoint_Pad_D1.0mm
- TP410: renamed from TP9; footprint jetson-orin-baseboard-footprints:TP_SMD_0.75mm -> TestPoint:TestPoint_Pad_D1.0mm
- TP411: renamed from TP11; footprint jetson-orin-baseboard-footprints:TP_SMD_0.75mm -> TestPoint:TestPoint_Pad_D1.0mm
- U402: renamed from U8; footprint jetson-orin-baseboard-footprints:IC_TPS65987DDHRSHR -> Fibel2:IC_TPS65987DDHRSHR; symbol jetson-orin-baseboard:TPS65988DHRSHR -> Fibel2:TPS65988DHRSHR
- renumbered D7 to D401, D8 to D402, D9 to D403, D10 to D404, D11 to D405, D12 to D406, D6 to D407, D13 to D408, D14 to D409, J8 to J401, J12 to J402, R37 to R414, U7 to U401, U9 to U403, U11 to U404, U12 to U405, U13 to U406, U14 to U407, U16 to U408, U10 to U409, U15 to U410, U17 to U411, U18 to U412
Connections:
- net GND: now also R431.1, R439.1, R463.1, R471.1
- net USB2_D_N: now also R470.2; no longer J402.A7 (D-), J402.B7 (D-), U412.4, U412.7
- net USB2_D_P: now also R469.2; no longer J402.A6 (D+), J402.B6 (D+), U412.2, U412.9
- net USBC0_CC1: now also R466.2, R471.2
- net USBC0_CC2: now also R463.2, R464.2
- net USBC0_VBUS: now also R472.2
- net USBC3_CC1: now also R431.2, R433.2
- net USBC3_CC2: now also R434.2, R439.2
- net USBC3_D_N: now also R427.1
- net USBC3_D_P: now also R428.1
- net USBC3_VBUS: now also R442.2
- new net: J402.A7 (D-), J402.B7 (D-), R468.1, R470.1, U412.4, U412.7
- new net: J402.A6 (D+), J402.B6 (D+), R467.1, R469.1, U412.2, U412.9
- new net CHG_DN: R468.2
- new net CHG_DP: R467.2
- new net USB0_D_N: R427.2
- new net USB0_D_P: R428.2
- new net VBUS_CHG: R464.1, R466.1, R472.1
- new net VBUS_USB0: R433.1, R434.1, R442.1
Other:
- note added: "Add VBUS_DET & TPS25820"
- note added: "Populate instead of whole FTDI for Type-C USB2.0"
- note added: "Populate instead of whole PD section for charging only"
- moved on the sheet: C404, C406, C407, C408, C409, C410, C411, C412, C413, C425, C426, C427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

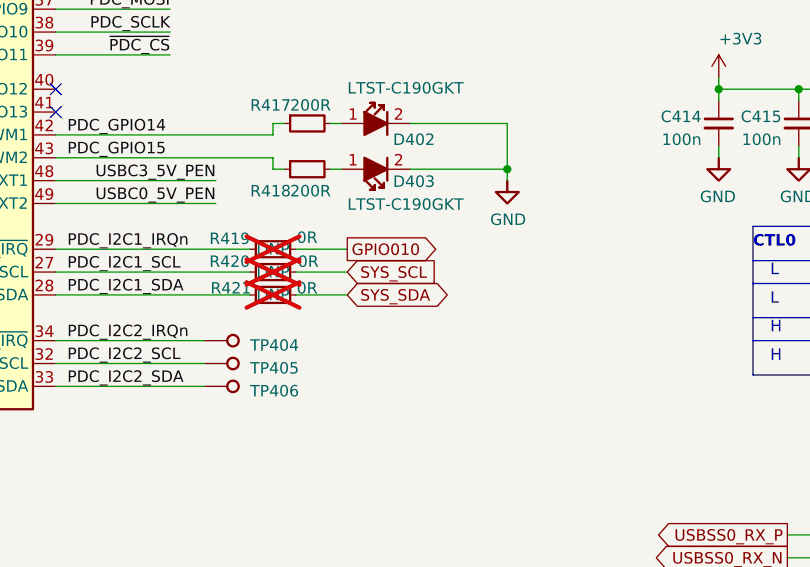
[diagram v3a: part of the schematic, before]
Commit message: continuing schematic work for pcie and other high speed interfaces
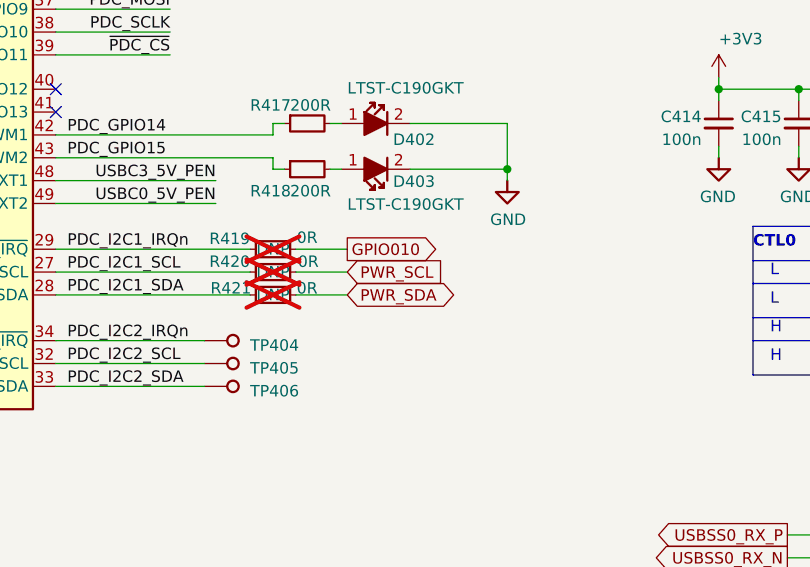
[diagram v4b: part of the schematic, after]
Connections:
- net SYS_SCL: no longer R420.1
- net SYS_SDA: no longer R421.1
- new net PWR_SCL: R420.1
- new net PWR_SDA: R421.1
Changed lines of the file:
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@@
 		)
 	)
-	(global_label "SYS_SCL"
+	(global_label "PWR_SCL"
 		(shape input)
 		(at 125.095 85.09 0)
@@
 		)
 	)
-	(global_label "SYS_SDA"
+	(global_label "PWR_SDA"
 		(shape bidirectional)
 		(at 125.095 87.63 0)

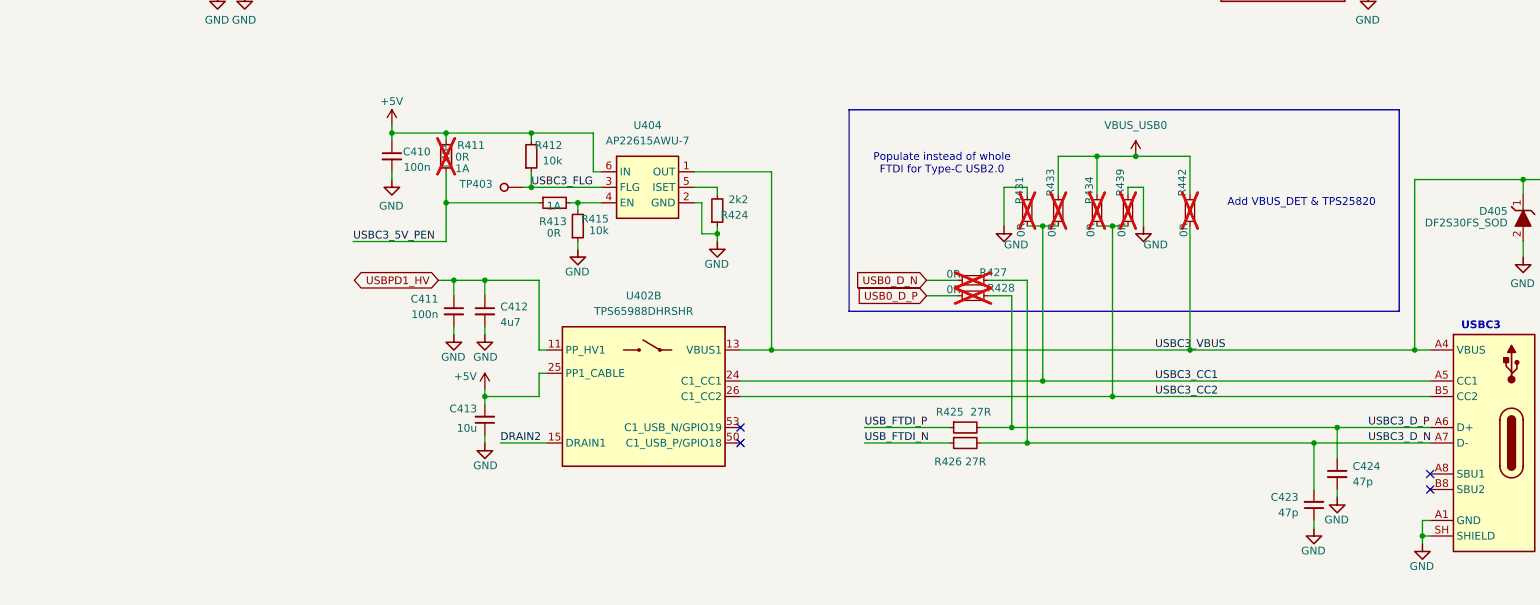
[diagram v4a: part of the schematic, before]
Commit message: restructured EPD side of things, replaced rp2040 with esp32 s3 because of it's LCD controller, USB, LP WIFI_BT & EPDiy compat, repurposed USB0 for ESP interfacing, added e-ink pmic
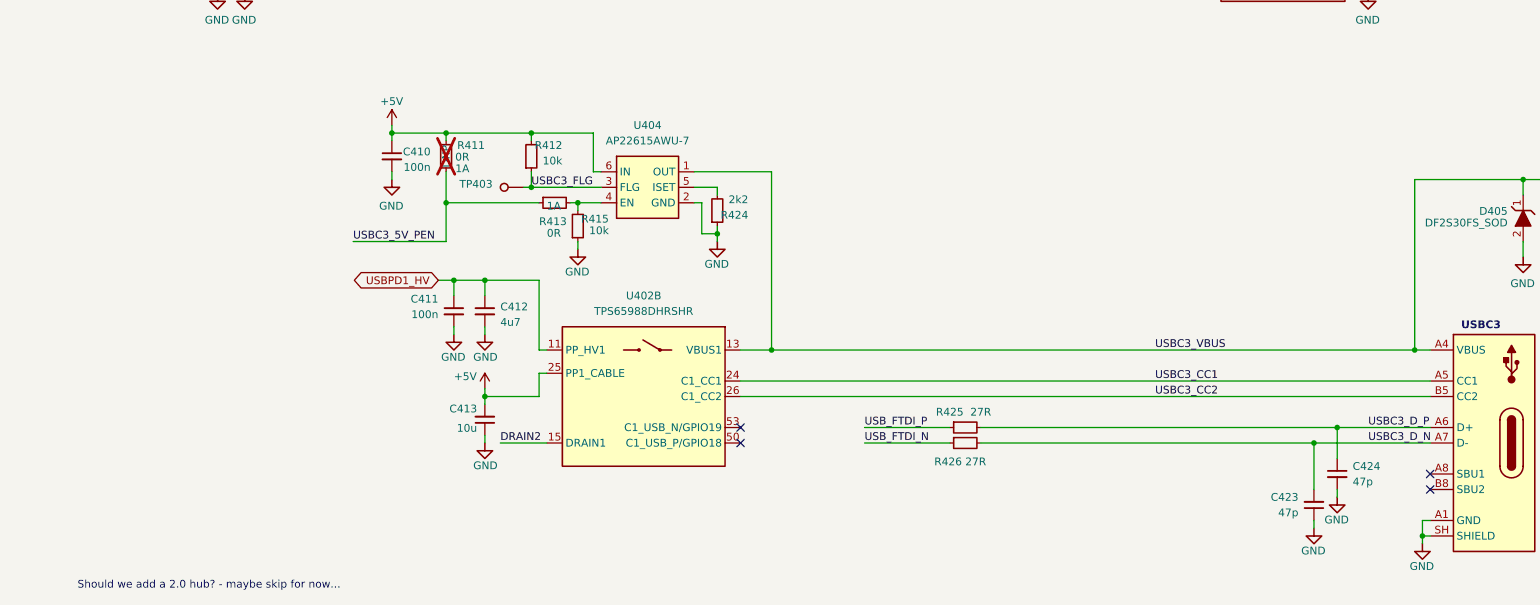
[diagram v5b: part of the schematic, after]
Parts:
- removed R427, R428, R431, R433, R434, R439, R442: 0R, Resistor_SMD:R_0603_1608Metric, symbol Device:R_Small
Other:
- note added: "Should we add a 2.0 hub? - maybe skip for now..."
- note removed: "Add VBUS_DET & TPS25820"
- note removed: "Populate instead of whole FTDI for Type-C USB2.0"
